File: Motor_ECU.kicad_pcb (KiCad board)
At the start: 2 copper layers, 61 x 61 mm, 65 parts, among them J1 Conn_01x04, J2 Conn_01x04, J3 Conn_01x02, J4 Debug, J5 Conn_01x02, U1 IFX9201SG, U2 TLE4964, U3 XMC1404_F064, U4 TLE7251, U5 LM35-D

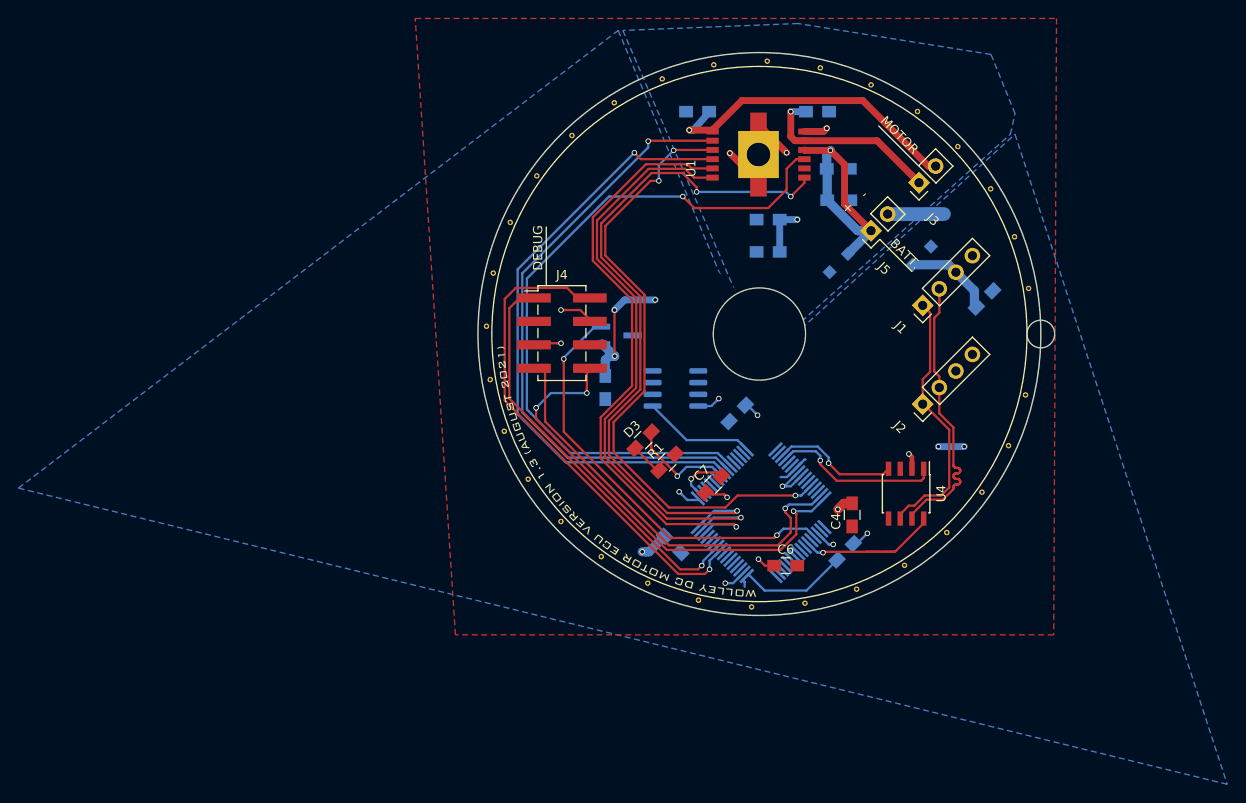
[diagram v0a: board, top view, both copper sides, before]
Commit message: Replace the 4-pin connectors with the new 5-pin connector
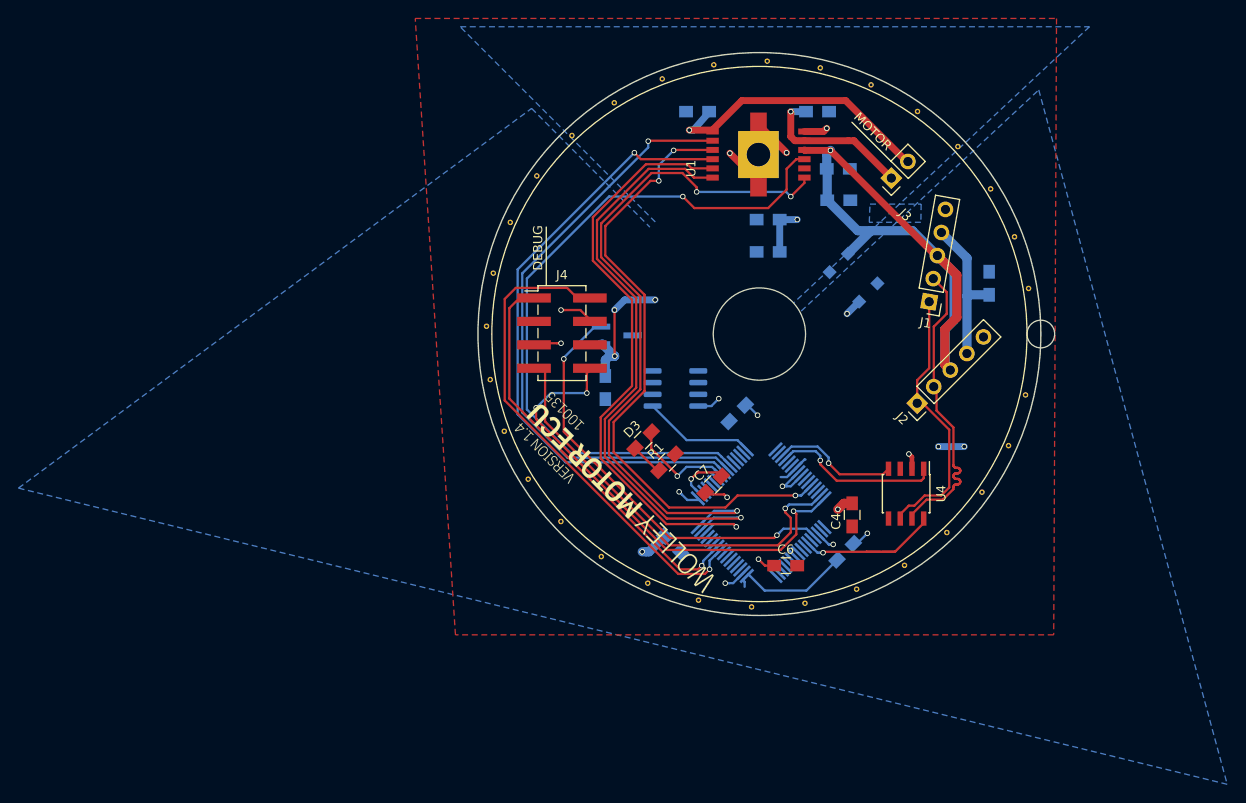
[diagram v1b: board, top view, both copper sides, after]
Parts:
- removed J5: Conn_01x02, Connector_PinHeader_2.54mm:PinHeader_1x02_P2.54mm_Vertical
- J1, J2: value Conn_01x04 -> Conn_01x05; footprint Pin_Headers:Pin_Header_Straight_1x04_Pitch2.54mm -> Connector_PinHeader_2.54mm:PinHeader_1x05_P2.54mm_Vertical
- R1: value R -> 1K2
- moved D1 7.05 mm to (143.6, 93.9)
- moved J3 3.04 mm to (146.1, 81.5)
- moved G*** 2.97 mm to (116.8, 116.2), turned to 135 degrees
- moved C5 1.77 mm to (156.7, 92.9), turned to 90 degrees
- moved J1 0.80 mm to (150.2, 94.9), turned to 170 degrees
- moved J2 0.61 mm to (148.9, 105.9)
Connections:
- J1 pad 3: +5V -> +BATT
- J1 pad 4: GND -> +5V
- J2 pad 3: +5V -> +BATT
- J2 pad 4: GND -> +5V
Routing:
- net +BATT: track 28.6 -> 70.6 mm
- net +5V: track 58.4 -> 67.4 mm, vias 14 -> 15
- net GND: track 59.8 -> 53.7 mm
- net MOTOR_OUT2: track 33.9 -> 30.7 mm
- net MOTOR_OUT1: track 20.3 -> 17.1 mm
- net CAN+: track 30.8 -> 32.9 mm
- net CAN-: track 28.7 -> 29.4 mm
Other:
- board text removed: "+"
- board text removed: "-"
- board text removed: "BATT."
